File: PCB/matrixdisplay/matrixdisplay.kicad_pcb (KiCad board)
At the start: 2 copper layers, 73 x 31 mm, 97 parts, among them J1 FILAS, J2 COLUMNAS, J3 SWD, J4 USART, J5 FILAS, J6 COL, SW1 BOOT0, SW2 P_ON, SW3 BT1, SW4 BT2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

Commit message: Modify buttons and mounting holes
BOOT0 was removed in favor of default boot mode
User Buttons replaced to horizontal aligment for easier access

Mounting Holes changed to M2 instead of M3 standard
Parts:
- removed SW1: BOOT0, Button_Switch_SMD:SW_SPST_B3U-1100P
- H1, H2: footprint MountingHole:MountingHole_3.2mm_M3 -> MountingHole:MountingHole_2mm
- SW3, SW4: footprint Button_Switch_SMD:SW_SPST_B3U-1100P -> SamacSys_Parts:TS24CA
- moved SW4 13.8 mm to (176.8, 104.2)
- moved SW3 12.0 mm to (162.4, 104.2)
- moved H2 1.45 mm to (183.4, 102.4)
- moved BT1 0.34 mm to (169.6, 81.0)
- moved G*** 0.25 mm to (167.6, 97.2)
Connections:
- R1 pad 1: Net-(SW1-B) -> GND
- SW3 pad 1: unconnected-(SW3-A-Pad1) -> Net-(U1-PF0)
- SW3 pad 2: Net-(SW3-B) -> GND
- SW4 pad 1: unconnected-(SW4-A-Pad1) -> Net-(U1-PF1)
- SW4 pad 2: Net-(SW4-B) -> GND
- U1 pad 2: Net-(SW3-B) -> Net-(U1-PF0)
- U1 pad 3: Net-(SW4-B) -> Net-(U1-PF1)
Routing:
- net Net-(U1-PF1): track 0.00 -> 68.9 mm
- net Net-(SW3-B): track 63.9 -> 0.00 mm
- net Net-(U1-PF0): track 0.00 -> 51.8 mm
- net Net-(SW4-B): track 50.5 -> 0.00 mm
- net +3.3V: track 100.8 -> 93.4 mm
- net Net-(SW1-B): track 6.32 -> 0.00 mm
- net GND: track 22.7 -> 21.3 mm
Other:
- board text added: "+"

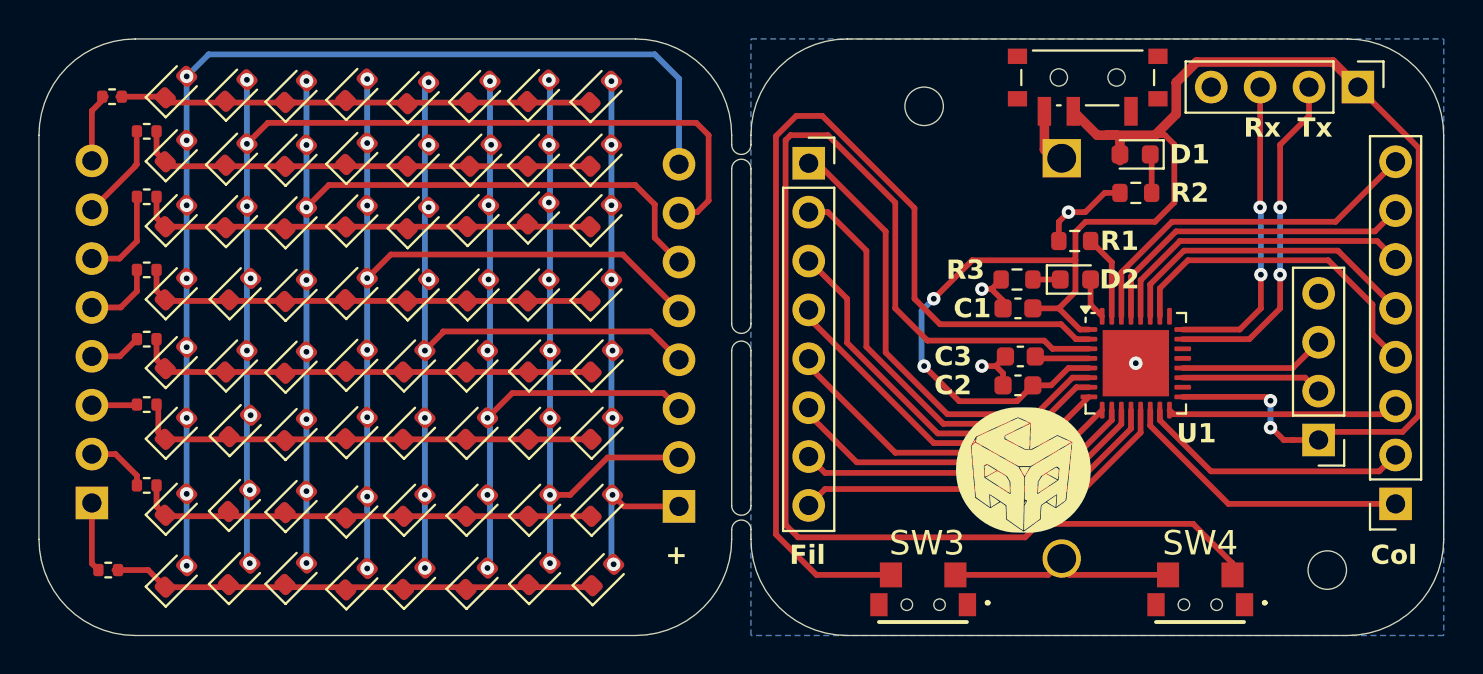
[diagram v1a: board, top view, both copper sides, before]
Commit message: fix (pcb): Correcion serigrafia SWD
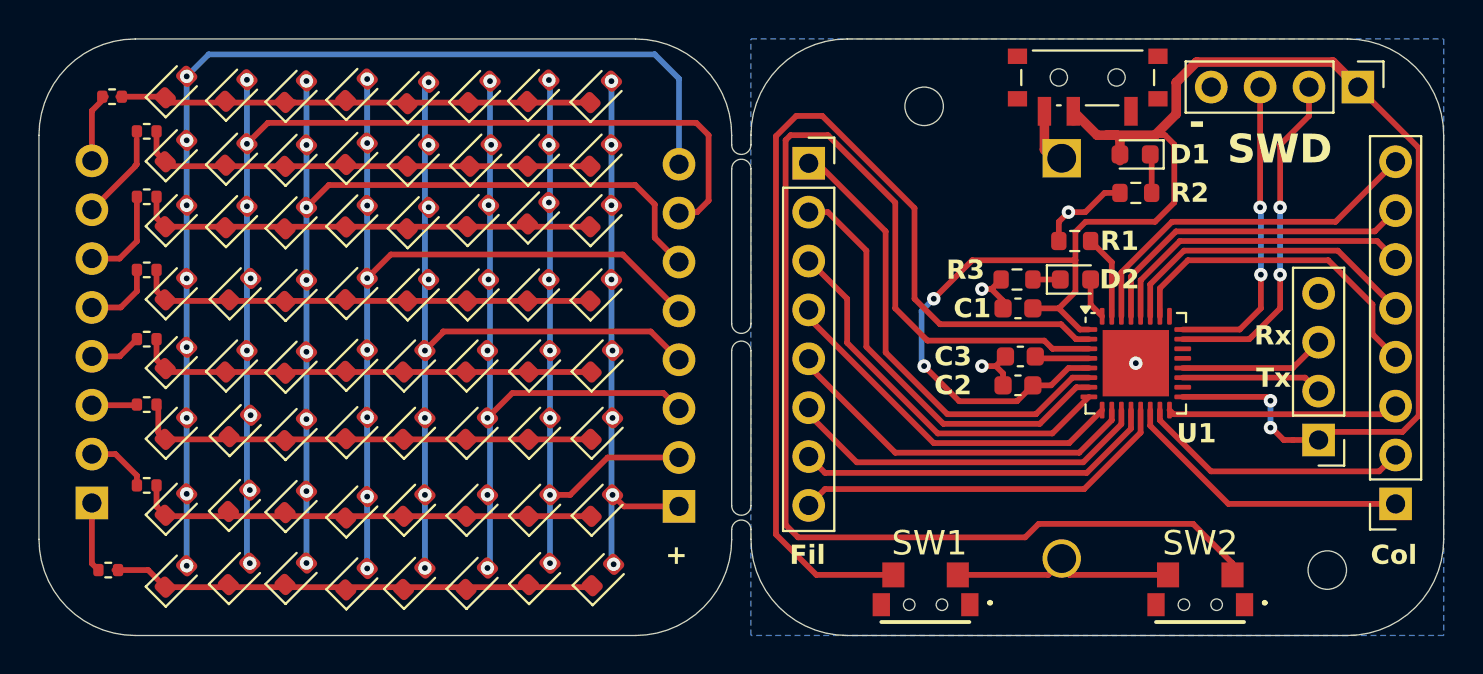
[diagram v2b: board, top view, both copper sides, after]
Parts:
- removed the G*** at (167.6, 97.2)
- moved SW1 0.12 mm to (162.5, 104.2)
- renumbered SW3 to SW1, SW4 to SW2
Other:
- board text added: "-"
- board text added: "SWD"
